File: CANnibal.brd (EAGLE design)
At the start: 15.2 x 36.2 mm, 22 parts, among them J1 POGOPIN-CONN-4, J3 455-1750-1-ND, J6 455-1750-1-ND, U1 STM32F042C6T6, U2 MF-REG-SOT235-3.3V-300mA

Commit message: Cleanup
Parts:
- moved C2 0.64 mm to (12.7, 22.2)
- moved DA1 0.64 mm to (7.62, 27.3)
- moved U$4 0.64 mm to (7.62, 1.91)
- moved U1 0.64 mm to (7.62, 17.1)
- moved U2 0.64 mm to (7.78, 9.84)
- moved F1 0.64 mm to (3.02, 8.26)
- moved J2 0.64 mm to (3.81, 34.3)
- moved C6 0.64 mm to (1.27, 14.8)
- moved J3 0.64 mm to (1.91, 24.8)
- moved LED2 0.64 mm to (1.27, 3.17)
- moved R2 0.64 mm to (1.27, 9.84)
- moved R4 0.64 mm to (1.27, 19.4)
- moved C1 0.63 mm to (12.4, 9.84)
- moved C3 0.63 mm to (4.29, 29.2)
- moved C4 0.63 mm to (2.54, 22.2)
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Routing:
- net N$3: track 3.02 -> 3.98 mm

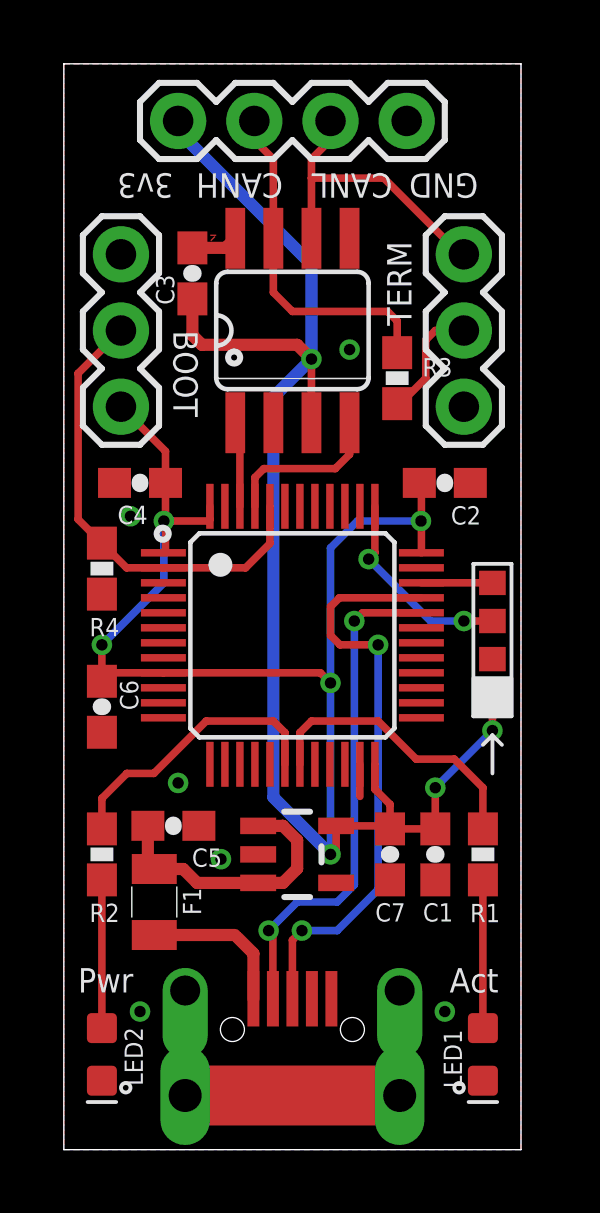
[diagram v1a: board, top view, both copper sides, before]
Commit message: Final version
Updates USB footprint, fiducials, images, etc
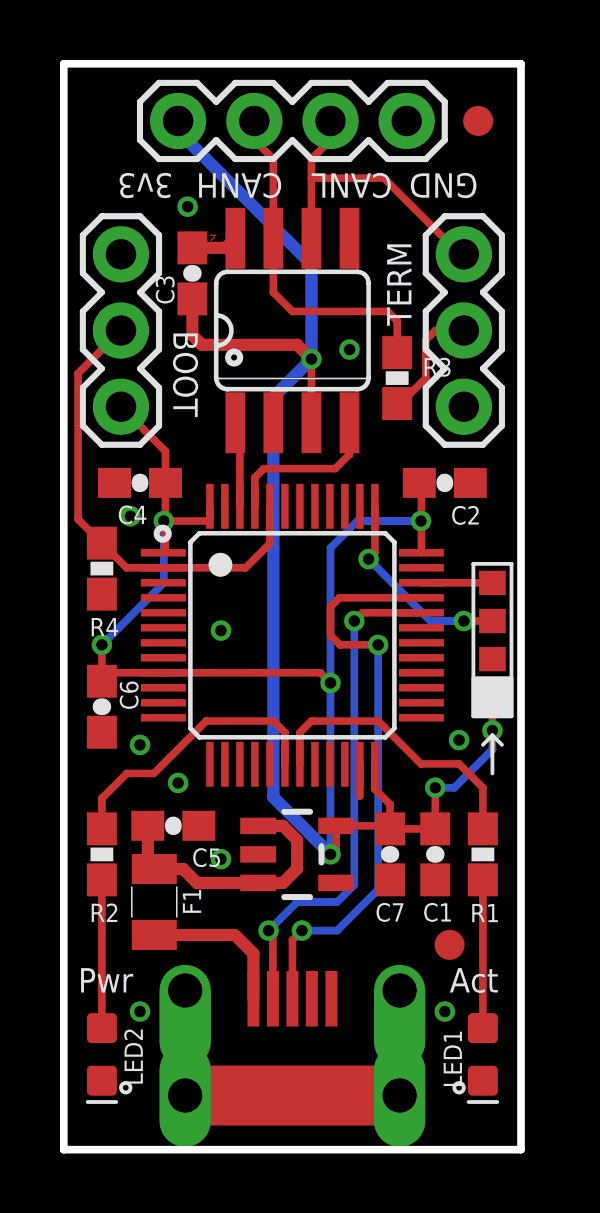
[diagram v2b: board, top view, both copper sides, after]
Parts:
- added FD1, FD2: FIDUCIAL1X2, SparkFun-Aesthetics:FIDUCIAL-1X2
- added LOGO1: OSHW-LOGOS, SparkFun-Aesthetics:OSHW-LOGO-S
- U$4: device micro usb B - 4LEGS:MICRO_USB_4_LEGS -> pmc_lib:MICRO_USB_4_LEGS
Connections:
- net GND: now also U2.4
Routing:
- net GND: vias 6 -> 10
